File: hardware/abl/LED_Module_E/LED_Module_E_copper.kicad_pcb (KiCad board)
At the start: 4 copper layers, 52 x 10 mm, 35 parts, among them K1 Conn_01x01, K10 Conn_01x01, K11 Conn_01x01, K12 Conn_01x01, K13 Conn_01x01, K14 Conn_01x01, K15 Conn_01x01, K16 Conn_01x01, K17 Conn_01x01, K18 Conn_01x01, K2 Conn_01x01, K3 Conn_01x01, K4 Conn_01x01, K5 Conn_01x01, K6 Conn_01x01, K7 Conn_01x01, K8 Conn_01x01, K9 Conn_01x01, U1 TMP1075DGK

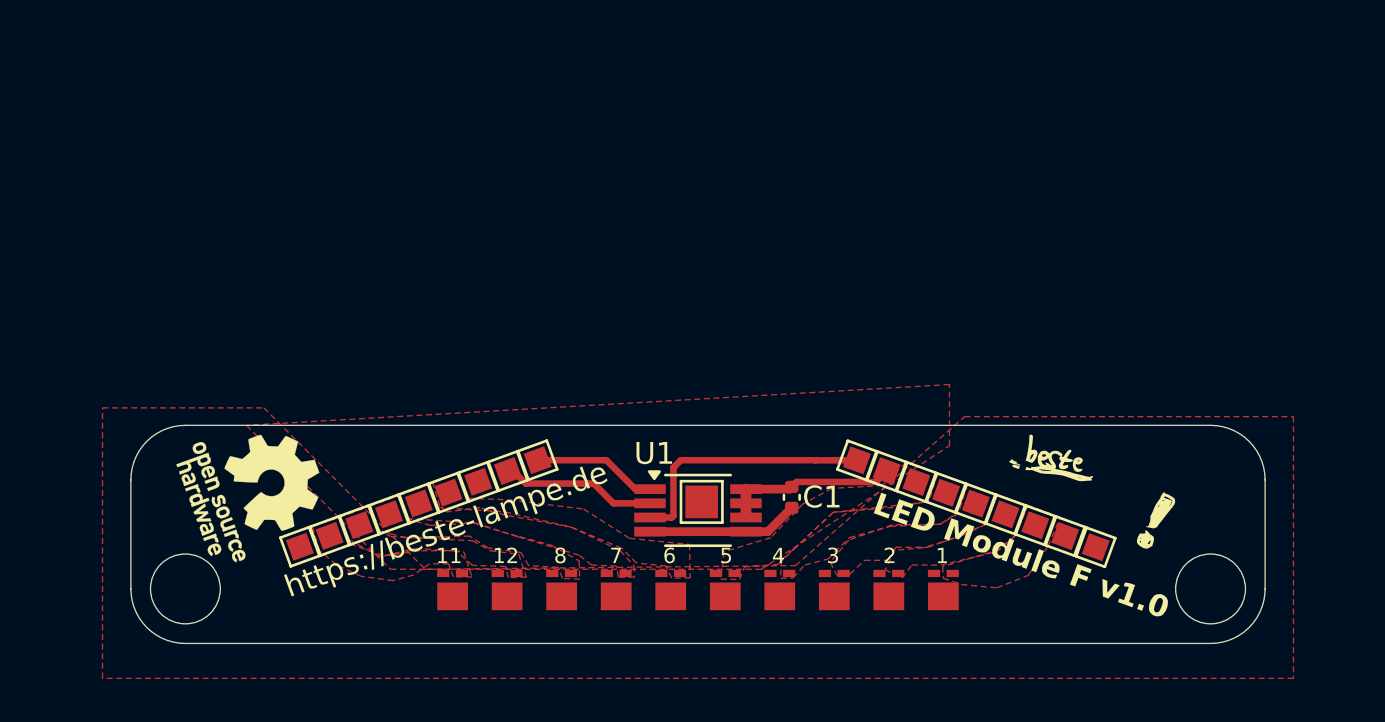
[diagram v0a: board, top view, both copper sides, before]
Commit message: Use full height for the copper PCB as well.
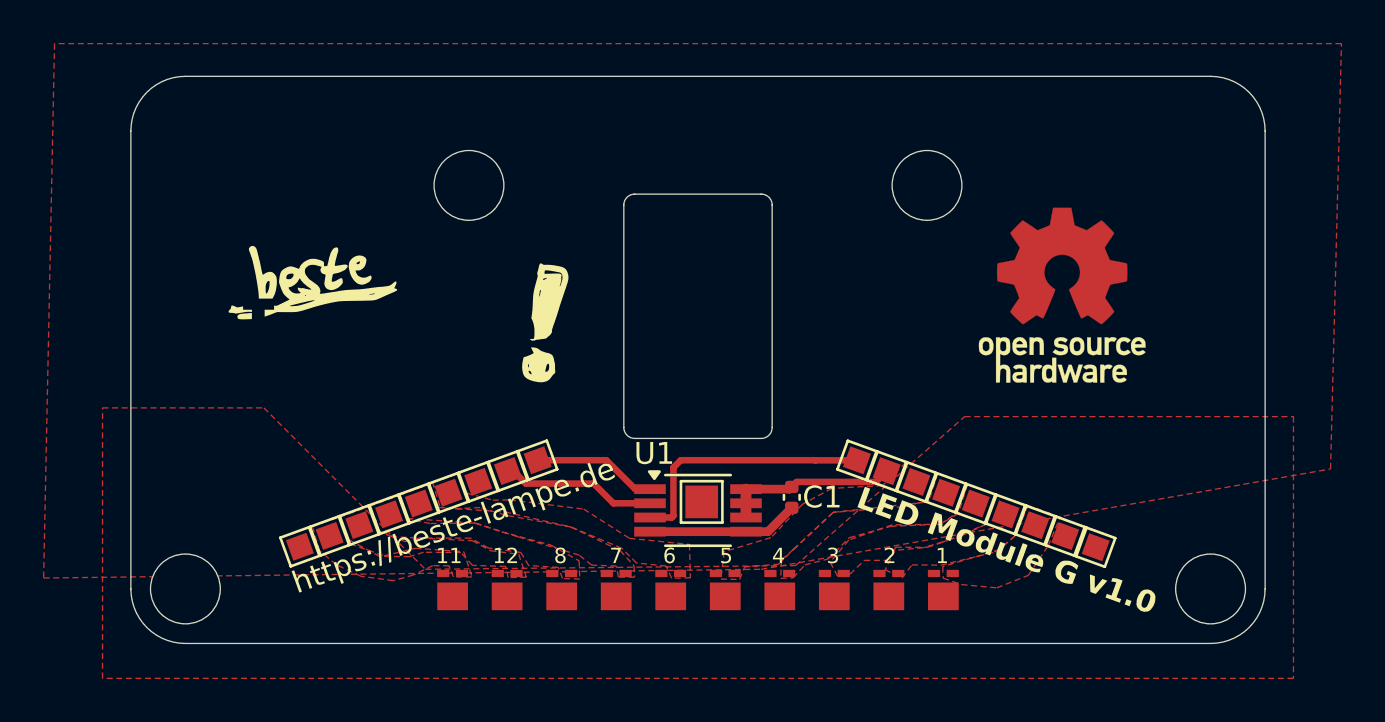
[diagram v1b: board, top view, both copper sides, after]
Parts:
- added H1: MountingHole, MountingHole:MountingHole_3.2mm_M3, F.Cu at (127.0, 62.0)
- added H4: MountingHole, MountingHole:MountingHole_3.2mm_M3, F.Cu at (148.0, 62.0)
- REF**: value OSHW-Logo_5.7x6mm_SilkScreen -> OSHW-Logo_7.5x8mm_Copper; footprint Symbol:OSHW-Logo_5.7x6mm_SilkScreen -> Symbol:OSHW-Logo_7.5x8mm_Copper
- moved REF** 38.0 mm to (154.2, 67.0), turned to 0 degrees
- moved G*** 32.7 mm to (124.0, 67.8), turned to 0 degrees
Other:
- board size 52 x 10 mm -> 52 x 26 mm
- board text added: "LED Module G v1.0"
- board text removed: "LED Module F v1.0"

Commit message: Several small fixes
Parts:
- D1, D11, D12, D2, D3, D4, D5, D6, D7, D8: footprint Cree XLAMP XE-G LED XEGAVT-H0:XEGAVTH_clean -> Cree XLAMP XE-G LED XEGAVT-H0:XEGAVTH_clean_bigger_solder

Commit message: Many small adjustments for the next production run.
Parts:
- removed the REF** at (137.7, 76.5)
- added H7: MountingHole_Pad, TestPoint:TestPoint_Pad_D2.5mm, F.Cu at (115.0, 63.0)
- added H8: MountingHole_Pad, TestPoint:TestPoint_Pad_D2.5mm, F.Cu at (160.0, 63.0)
- D1: value XEGAVT-H0-0000-000-000000K2001 -> XEGAWT-H2-0000-000-00000UT122G
- D11: value XEGAVT-H0-0000-000-000000K2001 -> XEGAWT-H2-0000-000-00000UT227H
- D12: value XEGAVT-H0-0000-000-000000K2001 -> XEGAAM-H2-0000-000-000000Q5001
- D2: value XEGAVT-H0-0000-000-000000K2001 -> XEGAAM-H2-0000-000-000000R4001
- D3: value XEGAVT-H0-0000-000-000000K2001 -> XEGAPB-H0-0000-000-000000Q5001
- D4: value XEGAVT-H0-0000-000-000000K2001 -> XEGAWT-H2-0000-000-00000UT650G
- D5: value XEGAVT-H0-0000-000-000000K2001 -> XEGAPA-H0-0000-000-000000T3001
- D6: value XEGAVT-H0-0000-000-000000K2001 -> XEGAPL-H0-0000-000-000000V3001
- D7: value XEGAVT-H0-0000-000-000000K2001 -> XEGAWT-H2-0000-000-00000UT330G
- D8: value XEGAVT-H0-0000-000-000000K2001 -> XEGAPO-H0-0000-000-000000S3001
- K1, K10, K11, K12, K13, K14, K15, K16, K17, K18, K2, K3, K4, K5, K6, K7, K8, K9: footprint TestPoint:TestPoint_Pad_1.0x1.0mm -> TestPoint:TestPoint_Pad_D1.5mm
- U1: footprint Package_SO:VSSOP-8_3.0x3.0mm_P0.65mm -> Package_SON:WSON-8-1EP_2x2mm_P0.5mm_EP0.9x1.6mm
- moved K9 7.20 mm to (136.5, 78.0), turned to 0 degrees
- moved K10 7.15 mm to (138.5, 78.0), turned to 0 degrees
- moved K8 6.41 mm to (134.5, 78.0), turned to 0 degrees
- moved K11 6.35 mm to (140.5, 78.0), turned to 0 degrees
- moved K7 5.62 mm to (132.5, 78.0), turned to 0 degrees
- moved K12 5.56 mm to (142.5, 78.0), turned to 0 degrees
- moved K6 4.83 mm to (130.5, 78.0), turned to 0 degrees
- moved K13 4.77 mm to (144.5, 78.0), turned to 0 degrees
- moved C1 4.33 mm to (139.4, 79.9), turned to 0 degrees
- moved K5 4.06 mm to (128.5, 78.0), turned to 0 degrees
- moved K14 4.00 mm to (146.5, 78.0), turned to 0 degrees
- moved U1 3.75 mm to (136.9, 80.6), turned to -90 degrees
- moved K4 3.29 mm to (126.5, 78.0), turned to 0 degrees
- moved K15 3.23 mm to (148.5, 78.0), turned to 0 degrees
- moved REF** 3.15 mm to (153.5, 70.1)
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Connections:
- K10 pad 1: /ALERT -> /SDA
- K8 pad 1: /SCL -> /ALERT
- K9 pad 1: /SDA -> /SCL
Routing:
- net /ALERT: track 11.9 -> 2.99 mm
- net /SCL: track 7.13 -> 1.92 mm
- net /SDA: track 5.73 -> 2.00 mm
- net GND: track 6.95 -> 9.69 mm
- net +3.3V: track 7.97 -> 6.51 mm
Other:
- board size 52 x 26 mm -> 52 x 28.5 mm
- board text added: "3.3V"
- board text added: "5V"
- board text added: "AL"
- board text added: "GND"
- board text added: "LED Module G v1.1"
- board text added: "SCL"
- board text added: "SDA"
- board text removed: "LED Module G v1.0"

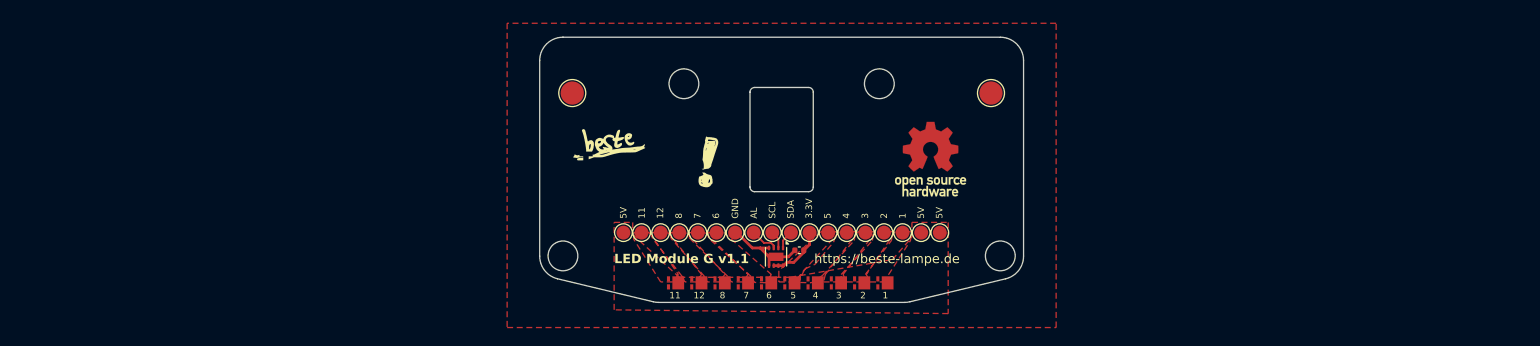
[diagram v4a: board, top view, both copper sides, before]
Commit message: Update files and documentation for LED modules E and G.
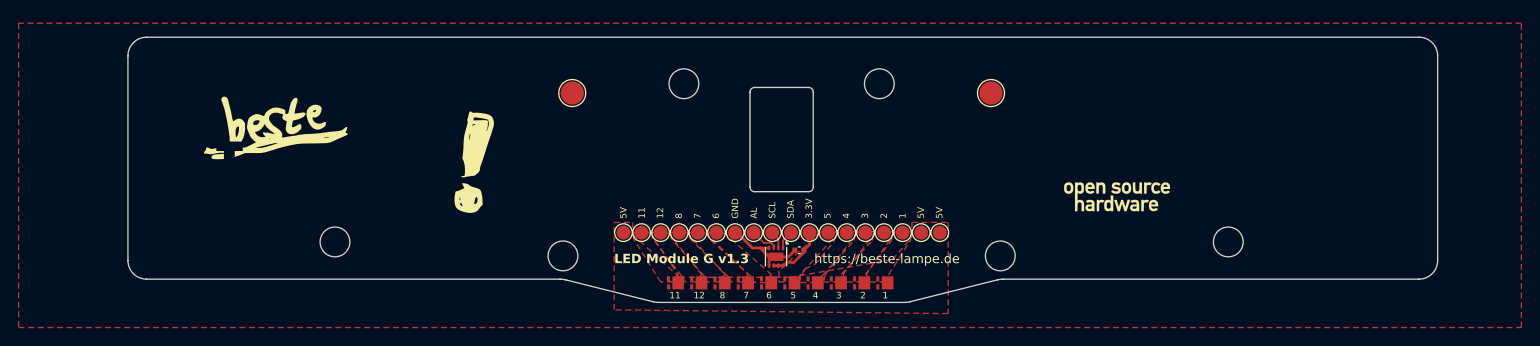
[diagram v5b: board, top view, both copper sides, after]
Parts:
- added H2: MountingHole, MountingHole:MountingHole_3.2mm_M3, F.Cu at (185.5, 79.0)
- added H3: MountingHole, MountingHole:MountingHole_3.2mm_M3, F.Cu at (89.5, 79.0)
- D1, D11, D12, D2, D3, D4, D5, D6, D7, D8: footprint Cree XLAMP XE-G LED XEGAVT-H0:XEGAVTH_clean_bigger_solder -> Cree XLAMP XE-G LED XEGAVT-H0:XEGAVTH_PCBA
- REF**: value OSHW-Logo_7.5x8mm_Copper -> OSHW-Logo_11.4x12mm_Copper; footprint Symbol:OSHW-Logo_7.5x8mm_Copper -> Symbol:OSHW-Logo_11.4x12mm_Copper
- U1: value TMP1075DGK -> TMP1075DSGR
- moved G*** 31.9 mm to (91.2, 69.5)
- moved REF** 20.0 mm to (173.5, 69.7)
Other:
- board size 52 x 28.5 mm -> 140.8 x 28.5 mm
- board text added: "LED Module G v1.3"
- board text removed: "LED Module G v1.1"

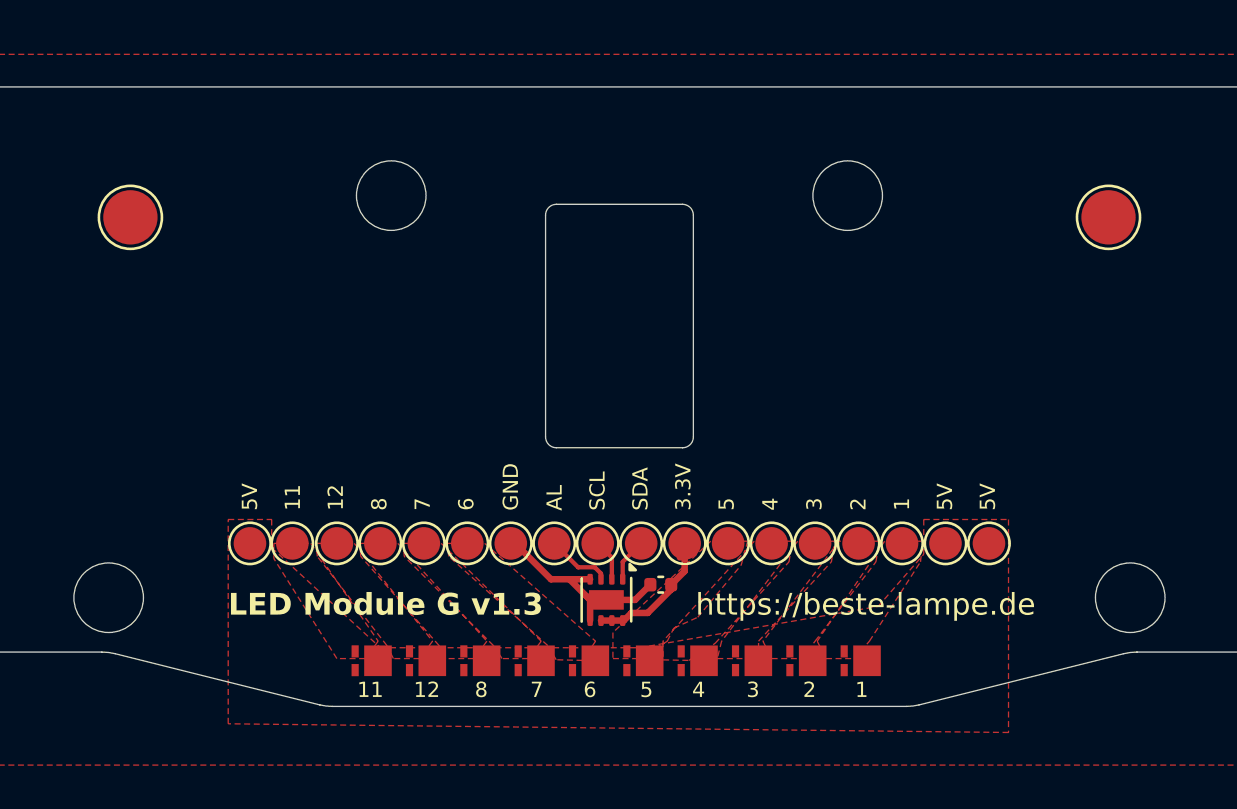
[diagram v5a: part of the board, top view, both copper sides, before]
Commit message: LED Module E version 4.0: two rows of castellated holes instead of one, for larger pitch and easier soldering. Also optimized routing.
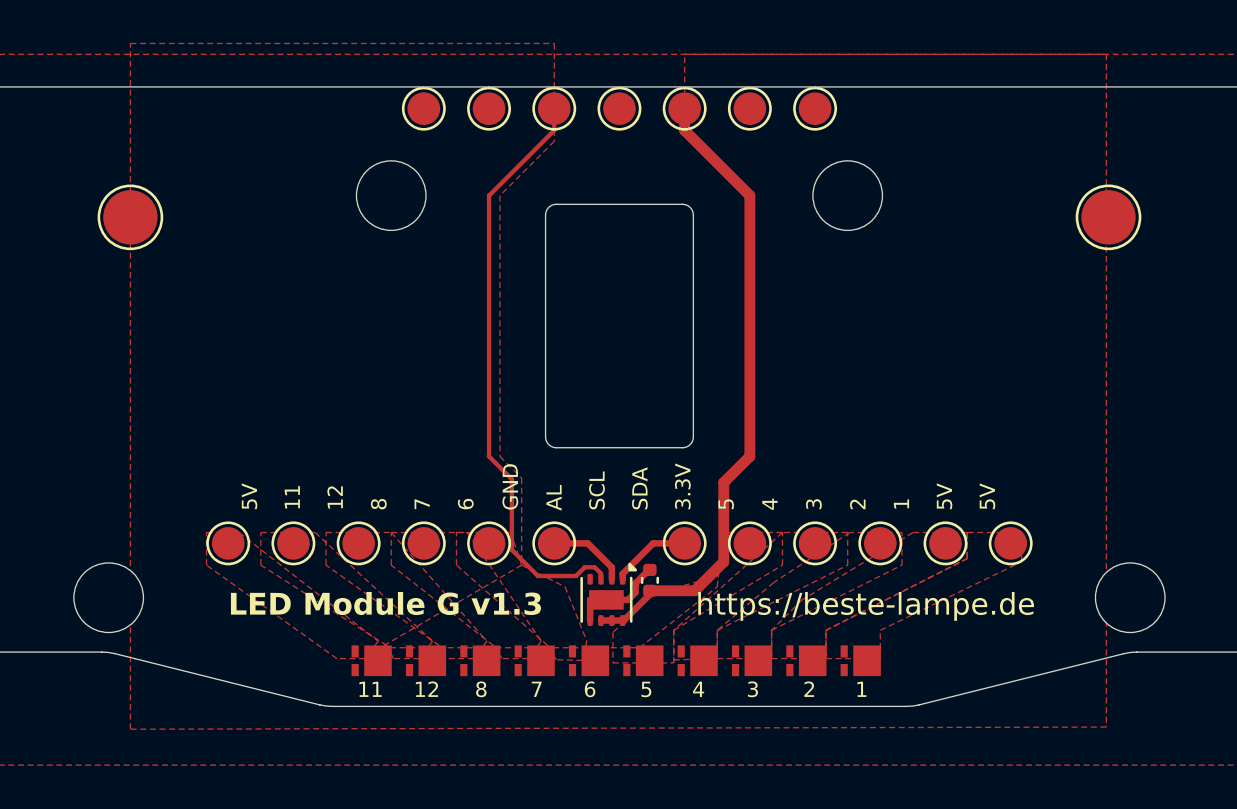
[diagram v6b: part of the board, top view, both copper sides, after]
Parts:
- added K1: Conn_01x01, TestPoint:TestPoint_Pad_D1.5mm, F.Cu at (131.5, 58.0)
- moved K17 21.9 mm to (143.5, 58.0)
- moved K1 21.5 mm to (128.5, 58.0)
- moved K18 21.5 mm to (146.5, 58.0)
- moved K7 20.6 mm to (137.5, 58.0)
- moved K11 20.0 mm to (140.5, 58.0)
- moved K8 20.0 mm to (134.5, 58.0)
- moved K16 5.00 mm to (155.5, 78.0)
- moved K15 4.00 mm to (152.5, 78.0)
- moved K14 3.00 mm to (149.5, 78.0)
- moved K2 2.95 mm to (119.5, 78.0)
- moved K10 2.00 mm to (140.5, 78.0)
- moved K13 2.00 mm to (146.5, 78.0)
- moved K3 2.00 mm to (122.5, 78.0)
- moved K9 2.00 mm to (134.5, 78.0)
- moved K12 1.00 mm to (143.5, 78.0)
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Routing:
- net /ALERT: track 2.99 -> 27.1 mm
- net +3.3V: track 6.51 -> 29.6 mm
- net GND: track 9.69 -> 4.52 mm
- net /SCL: track 1.92 -> 3.65 mm
- net /SDA: track 2.00 -> 3.68 mm
